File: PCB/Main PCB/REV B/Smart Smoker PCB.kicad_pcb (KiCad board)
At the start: 4 copper layers, 6.3 x 2.1 mm, 143 parts, among them J1 393570002, J2 Conn_01x03_Female, J3 1051330001, J4 393570002, J5 393570002, J6 393570002, J7 Hopper, J8 Lid, Q1 2N7002, Q2 2N7002, Q3 MBT3904DW1, Q4 2N7002, U1 AMS1117-3.3, U10 ALDP105W, U11 TLP2362TPR_E, U12 ALDP105W, U13 STM811SW16F, U2 TS5A23159DGS, U3 ESP32-WROOM-32UE_16MB, U4 MAX31855KASA, U5 TPS2115APWR, U6 TLP2362TPR_E, U7 ALDP105W, U8 CP2102N-A02-GQFN24, U9 TLP2362TPR_E

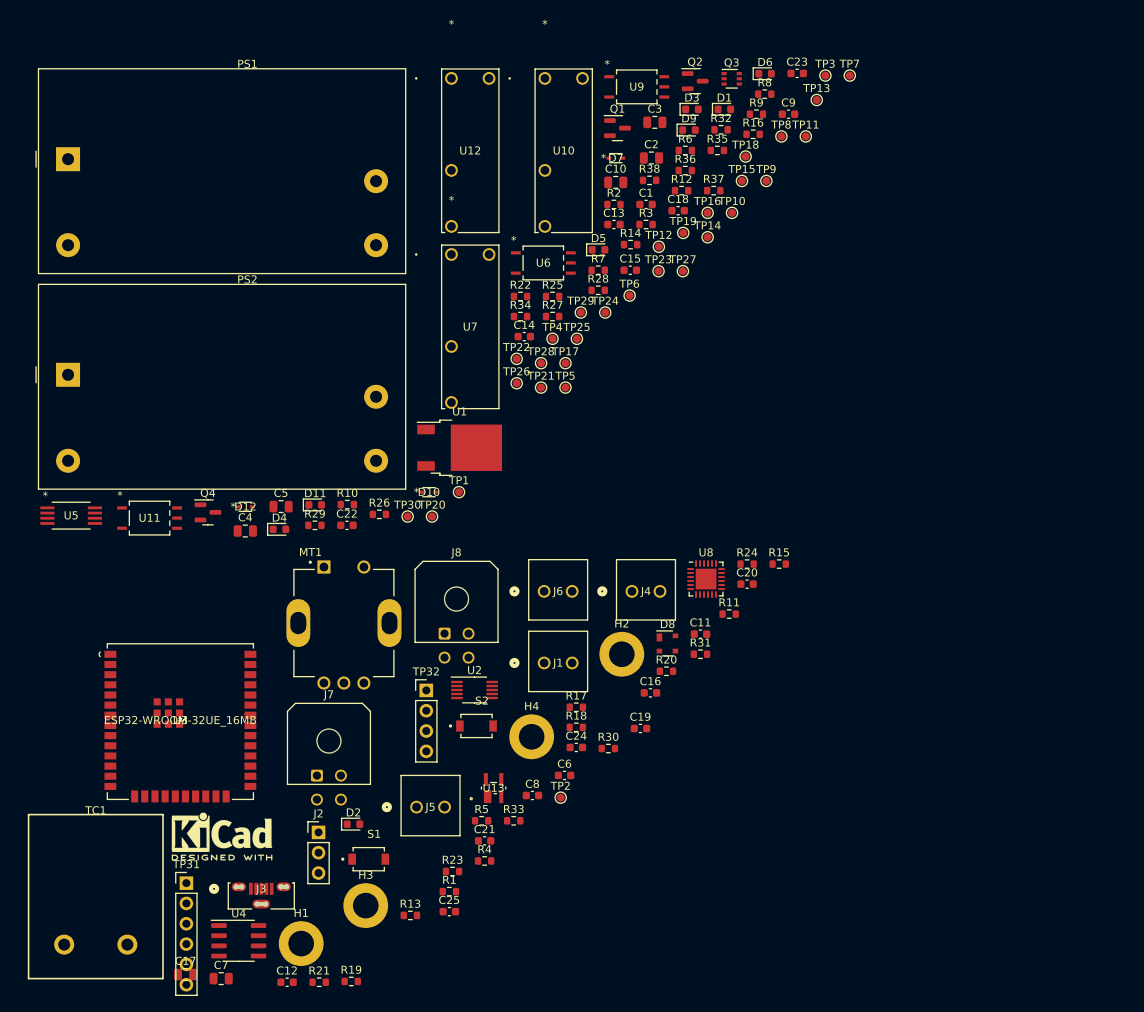
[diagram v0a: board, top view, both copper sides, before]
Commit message: PCB schematic updates, Delete lid connections, add qwiic connectors
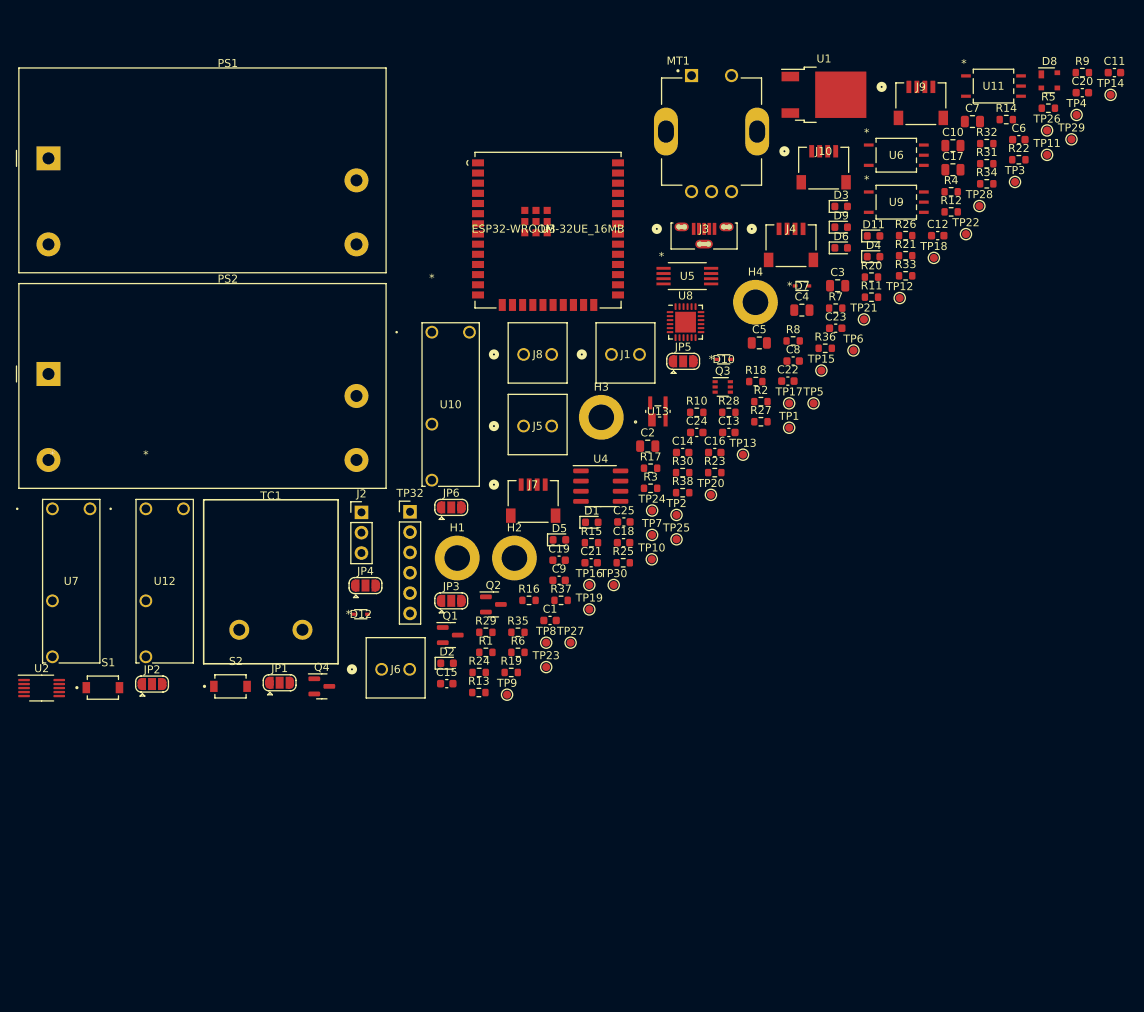
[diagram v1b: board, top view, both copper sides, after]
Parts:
- removed AE1: Antenna, Symbol:KiCad-Logo2_5mm_SilkScreen
- removed TP31: GPIO MISC., Connector_PinHeader_2.54mm:PinHeader_1x06_P2.54mm_Vertical
- added J10: Spare2, Customs Smoker:PRT-14417, F.Cu at (115.2, 27.5)
- added J9: Spare1, Customs Smoker:PRT-14417, F.Cu at (127.4, 19.4)
- added JP1: SolderJumper_3_Open, Jumper:SolderJumper-3_P1.3mm_Open_RoundedPad1.0x1.5mm, F.Cu at (47.2, 91.8)
- added JP2: SolderJumper_3_Open, Jumper:SolderJumper-3_P1.3mm_Open_RoundedPad1.0x1.5mm, F.Cu at (31.2, 92.0)
- added JP3: SolderJumper_3_Open, Jumper:SolderJumper-3_P1.3mm_Open_RoundedPad1.0x1.5mm, F.Cu at (68.7, 81.5)
- added JP4: SolderJumper_3_Open, Jumper:SolderJumper-3_P1.3mm_Open_RoundedPad1.0x1.5mm, F.Cu at (57.9, 79.6)
- added JP5: SolderJumper_3_Open, Jumper:SolderJumper-3_P1.3mm_Open_RoundedPad1.0x1.5mm, F.Cu at (97.6, 51.6)
- added JP6: SolderJumper_3_Open, Jumper:SolderJumper-3_P1.3mm_Open_RoundedPad1.0x1.5mm, F.Cu at (68.7, 69.9)
- J4: value 393570002 -> Hopper; footprint Customs Smoker:CONN_393570002_MOL -> Customs Smoker:PRT-14417
- J7: value Hopper -> Screen; footprint Connector_Molex:Molex_Micro-Fit_3.0_43045-0400_2x02_P3.00mm_Horizontal -> Customs Smoker:PRT-14417
- J8: value Lid -> 393570002; footprint Connector_Molex:Molex_Micro-Fit_3.0_43045-0400_2x02_P3.00mm_Horizontal -> Customs Smoker:CONN_393570002_MOL
- R34: value 10K 1% 0603 -> 0 Ohm 0603
- R36: value 0 Ohm 0603 -> 10K 1% 0603
- TP32: value Screen I2C -> GPIO MISC.; footprint Connector_PinHeader_2.54mm:PinHeader_1x04_P2.54mm_Vertical -> Connector_PinHeader_2.54mm:PinHeader_1x06_P2.54mm_Vertical
- moved C7 142.5 mm to (133.8, 21.6)
- moved C17 139.0 mm to (131.4, 27.7)
- moved C12 123.8 mm to (129.5, 35.9)
- moved U11 118.5 mm to (136.4, 17.2)
- moved R21 116.7 mm to (125.5, 38.4)
- moved R5 113.8 mm to (143.3, 20.0)
- moved R4 102.0 mm to (131.1, 30.4)
- moved J3 99.3 mm to (100.3, 35.9)
- moved C6 97.7 mm to (139.6, 23.9)
- moved C11 87.2 mm to (151.6, 15.5)
- moved D8 85.0 mm to (143.4, 16.5)
- moved R33 83.9 mm to (125.5, 40.9)
- moved U5 82.6 mm to (98.2, 41.0)
- moved D4 81.7 mm to (121.4, 38.5)
- moved D11 77.5 mm to (121.4, 35.9)
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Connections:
- J4 pad 1: /Auger_+ -> +5V
- J4 pad 2: /Auger_- -> +3.3V
- J5 pad 1: /Fan_+ -> /Auger_+
- J5 pad 2: /Fan_- -> /Auger_-
- J6 pad 1: /Ignitor_+ -> /Fan_+
- J6 pad 2: /Ignitor_- -> /Fan_-
- J7 pad 1: /I2C_SDA -> +5V
- J7 pad 2: +5V -> +3.3V
- J7 pad 3: /I2C_SCL -> /I2C_SDA
- J7 pad 4: +3.3V -> /I2C_SCL
- J8 pad 1: /I2C_SDA -> /Ignitor_+
- J8 pad 2: +5V -> /Ignitor_-
- Q3 pad 2: Net-(R30-Pad2) -> Net-(R28-Pad2)
- R28 pad 1: /IO13 -> /DTR
- R28 pad 2: Net-(JP1-Pad2) (its old number) -> Net-(R28-Pad2)
- R29 pad 1: /IO27 -> /IO13
- R30 pad 1: /DTR -> /IO27
- R30 pad 2: Net-(R30-Pad2) -> Net-(JP2-Pad2)
- R34 pad 1: /IO12 -> Net-(D12-Pad2)
- R34 pad 2: Net-(JP3-Pad2) (its old number) -> Net-(D11-Pad1)
- R35 pad 1: /IO26 -> /IO12
- R36 pad 1: Net-(D12-Pad2) -> /IO26
- R36 pad 2: Net-(D11-Pad1) -> Net-(JP4-Pad2)
- TP22 pad 1: /IO13 -> /DTR
- TP23 pad 1: /IO27 -> /IO13
- TP24 pad 1: /DTR -> /IO27
- TP32 pad 1: /I2C_SDA -> /IO25
- TP32 pad 2: /I2C_SCL -> /IO26
- TP32 pad 3: +5V -> /IO27
- TP32 pad 4: +3.3V -> /IO14

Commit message: PCB Layout - Begin Grouping of main PCB
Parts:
- moved C15 192.7 mm to (259.0, 66.0)
- moved S1 184.3 mm to (202.5, 142.5)
- moved PS1 182.8 mm to (187.8, 94.5)
- moved D2 182.0 mm to (243.6, 41.0)
- moved S2 181.3 mm to (213.8, 147.5)
- moved R6 180.0 mm to (249.6, 37.0), turned to 180 degrees
- moved TP16 177.0 mm to (262.0, 62.0)
- moved C5 172.9 mm to (280.0, 46.0), turned to -90 degrees
- moved PS2 169.5 mm to (187.8, 53.5)
- moved D5 165.0 mm to (243.4, 39.0)
- moved C4 163.5 mm to (276.0, 46.0), turned to -90 degrees
- moved U1 162.7 mm to (276.5, 39.5)
- moved D1 161.6 mm to (243.6, 35.0)
- moved C14 161.2 mm to (258.8, 64.0)
- moved R3 158.3 mm to (249.6, 41.0), turned to 180 degrees
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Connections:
- C1 pad 1: +5V -> GND
- C10 pad 2: +5V -> GND
- C11 pad 2: +5V -> GND
- C13 pad 2: +5V -> GND
- C14 pad 1: +5V -> GND
- C15 pad 1: +5V -> GND
- C16 pad 1: +5V -> GND
- C17 pad 1: +5V -> GND
- C18 pad 2: Net-(C18-Pad2) -> GND
- C19 pad 2: +5V -> GND
- C2 pad 2: +5V -> GND
- C20 pad 2: +5V -> GND
- C21 pad 2: +5V -> GND
- C22 pad 2: Net-(C22-Pad2) -> GND
- C23 pad 2: Net-(C23-Pad2) -> GND
- C24 pad 1: +5V -> GND
- C25 pad 2: +5V -> GND
- C3 pad 2: +5V -> GND
- C4 pad 2: +5V -> GND
- C5 pad 2: +5V -> GND
- C6 pad 1: +5V -> GND
- C7 pad 1: +5V -> GND
- C8 pad 1: +5V -> GND
- C9 pad 1: +5V -> GND
- D1 pad 1: /IO17 -> GND
- D2 pad 1: +5V -> GND
- D3 pad 1: +5V -> GND
- D4 pad 1: +5V -> GND
- D5 pad 1: /IO17 -> GND
- D8 pad 1: +5V -> GND
- J10 pad 1: +5V -> GND
- J3 pad 5: +5V -> GND
- J4 pad 1: +5V -> GND
- J7 pad 1: +5V -> GND
- J9 pad 1: +5V -> GND
- JP1 pad 1: +5V -> GND
- JP2 pad 1: +5V -> GND
- JP3 pad 1: +5V -> GND
- JP4 pad 1: +5V -> GND
- JP5 pad 1: +5V -> GND
- JP6 pad 1: +5V -> GND
- MT1 pad 1: +5V -> GND
- MT1 pad COM: +5V -> GND
- MT1 pad S1: +5V -> GND
- MT1 pad S2: +5V -> GND
- PS1 pad 3: +5V -> GND
- PS2 pad 3: +5V -> GND
- Q1 pad 3: +5V -> GND
- Q2 pad 3: +5V -> GND
- Q4 pad 3: +5V -> GND
- R1 pad 2: +5V -> GND
- R10 pad 2: +5V -> GND
- R23 pad 1: +5V -> GND
- R9 pad 1: +5V -> GND
- S1 pad 2: +5V -> GND
- S2 pad 1: +5V -> GND
- TP20 pad 1: +5V -> GND
- U1 pad 1: +5V -> GND
- U11 pad 3: +5V -> GND
- U11 pad 4: Net-(C23-Pad2) -> GND
- U13 pad 1: +5V -> GND
- U2 pad 3: +5V -> GND
- U3 pad 1: +5V -> GND
- U3 pad 15: +5V -> GND
- U3 pad 38: +5V -> GND
- U3 pad 39: +5V -> GND
- U3 pad 40: +5V -> GND
- U3 pad 41: +5V -> GND
- U3 pad 42: +5V -> GND
- U3 pad 43: +5V -> GND
- U3 pad 44: +5V -> GND
- U3 pad 45: +5V -> GND
- U3 pad 46: +5V -> GND
- U3 pad 47: +5V -> GND
- U4 pad 1: +5V -> GND
- U5 pad 3: +5V -> GND
- U5 pad 5: +5V -> GND
- U6 pad 3: +5V -> GND
- U6 pad 4: Net-(C18-Pad2) -> GND
- U8 pad 2: +5V -> GND
- U8 pad 25: +5V -> GND
- U9 pad 3: +5V -> GND
- U9 pad 4: Net-(C22-Pad2) -> GND

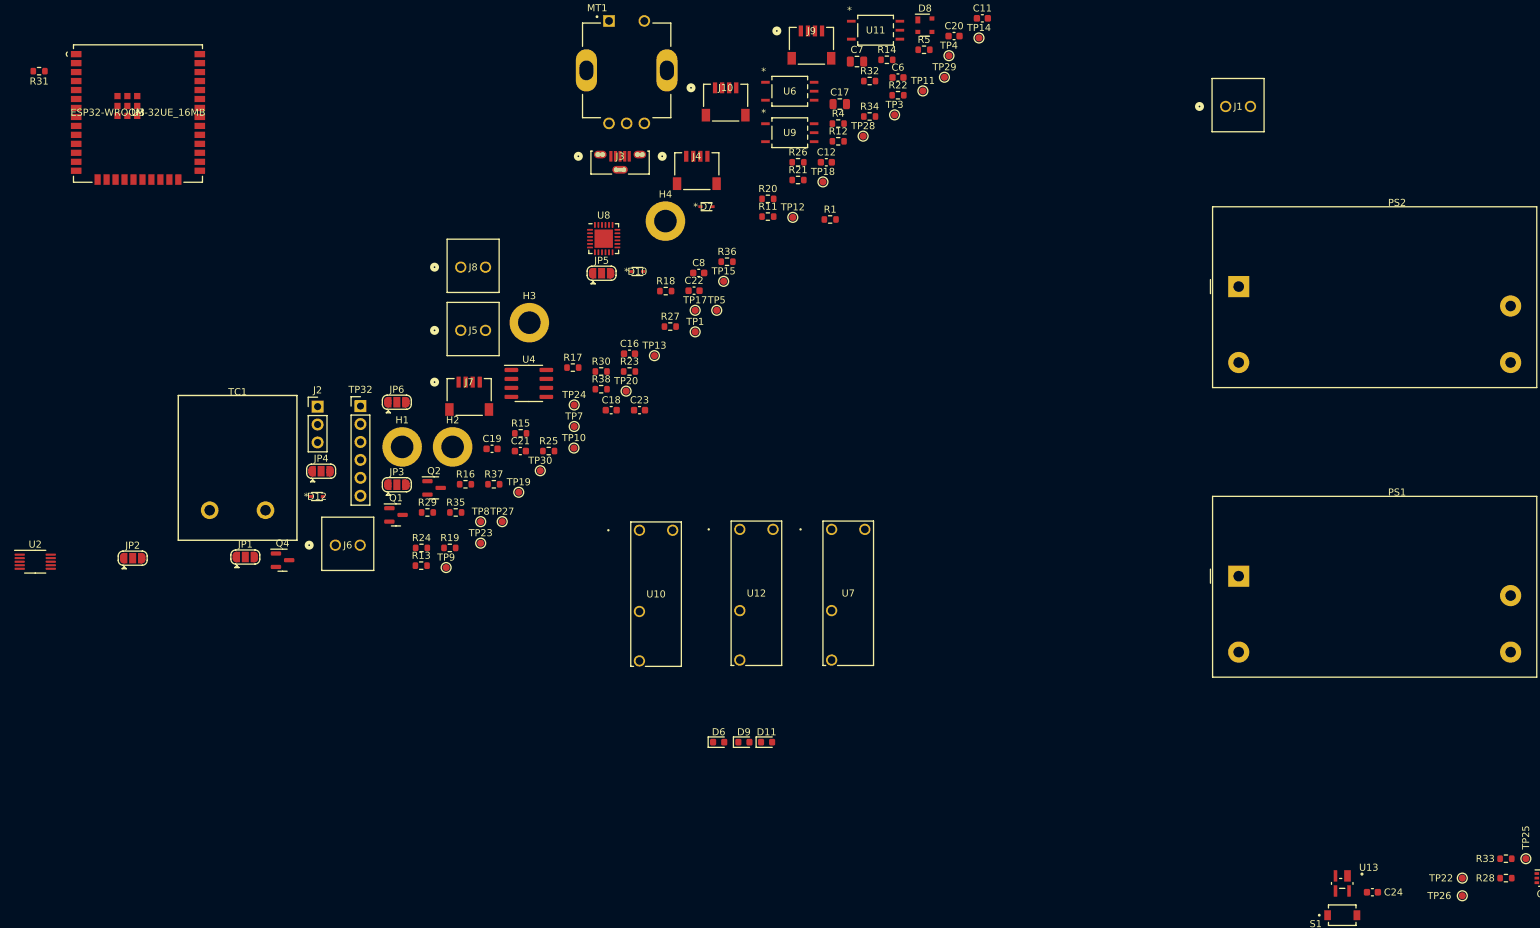
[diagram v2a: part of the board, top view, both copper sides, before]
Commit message: PCB Layout - Continue Grouping layout
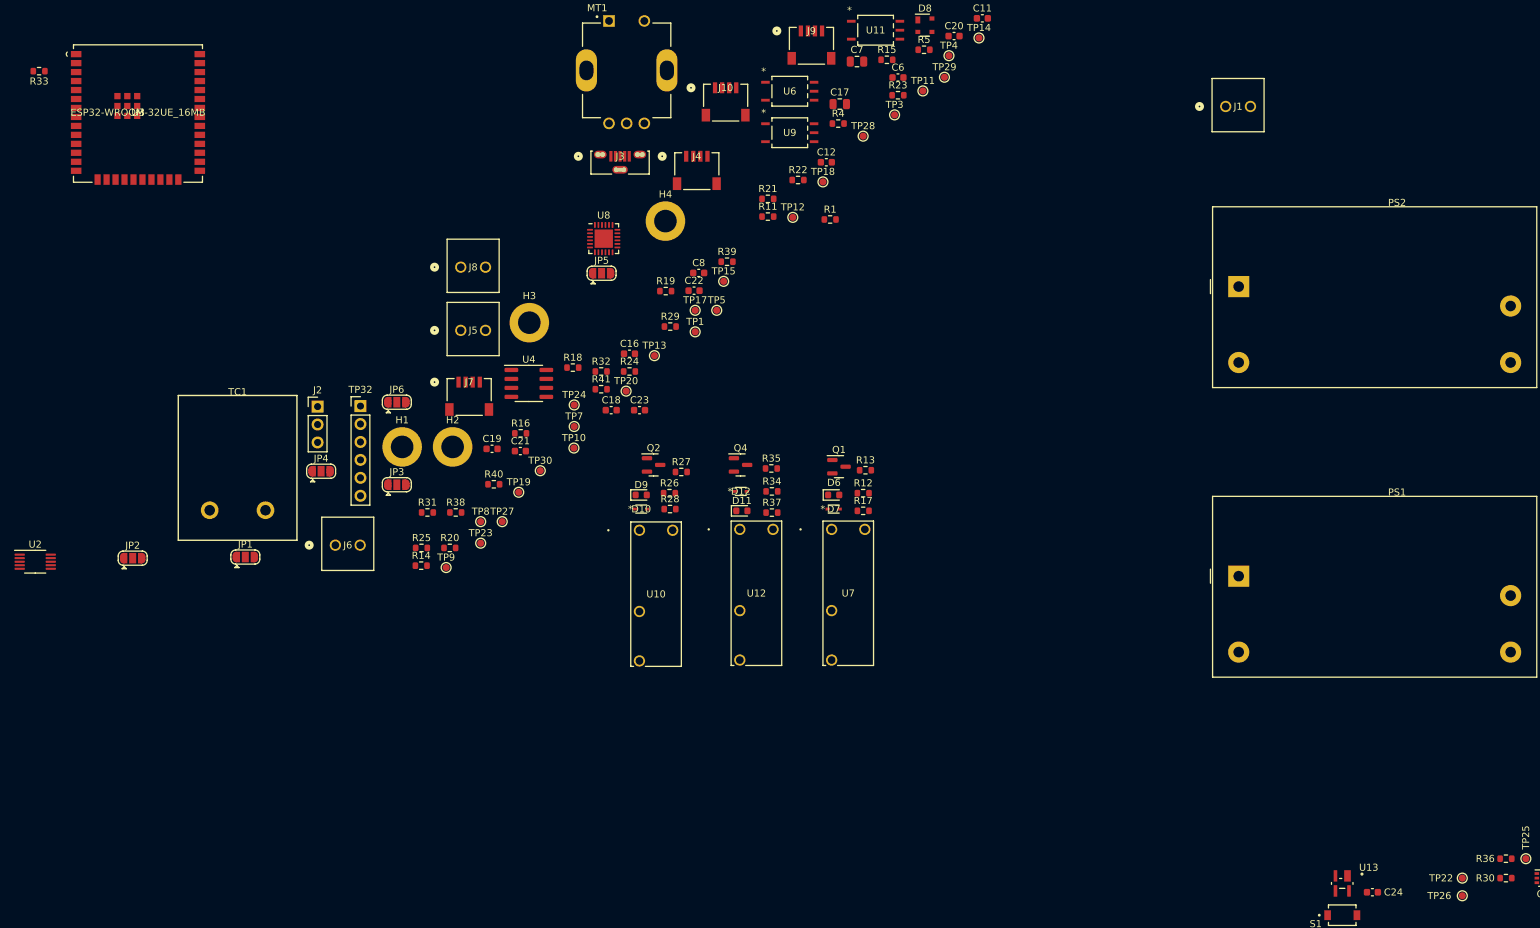
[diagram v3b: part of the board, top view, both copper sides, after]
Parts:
- added R13: 10K 1% 0603, Resistor_SMD:R_0603_1608Metric, F.Cu at (135.0, 79.5)
- added R27: 10K 1% 0603, Resistor_SMD:R_0603_1608Metric, F.Cu at (108.9, 79.8)
- added R35: 10K 1% 0603, Resistor_SMD:R_0603_1608Metric, F.Cu at (121.7, 79.2)
- moved Q4 66.2 mm to (117.3, 78.8)
- moved Q1 63.1 mm to (131.2, 79.0)
- moved D12 60.0 mm to (117.4, 82.5)
- moved R34 59.7 mm to (121.8, 82.5)
- moved R37 57.8 mm to (121.8, 85.5)
- moved R17 56.4 mm to (134.7, 85.2)
- moved R28 52.3 mm to (107.3, 85.0)
- moved R12 49.9 mm to (134.7, 82.8)
- moved D7 46.4 mm to (130.5, 85.0)
- moved D6 38.6 mm to (130.5, 83.0)
- moved D9 37.9 mm to (103.2, 83.0)
- moved D10 33.6 mm to (103.2, 85.0)
- moved D11 32.9 mm to (117.5, 85.2)
- moved Q2 31.2 mm to (105.0, 78.8)
- moved R26 18.1 mm to (107.2, 82.8)
- renumbered R13 to R14, R14 to R15, R15 to R16, R16 to R17, R17 to R18, R18 to R19, R19 to R20, R20 to R21, R21 to R22, R22 to R23, R23 to R24, R24 to R25, R25 to R26, R26 to R28, R27 to R29, R28 to R30, R29 to R31, R30 to R32, R31 to R33, R32 to R34, R33 to R36, R34 to R37, R35 to R38, R36 to R39, R37 to R40, R38 to R41
